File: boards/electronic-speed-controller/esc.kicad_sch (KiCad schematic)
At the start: 29 parts, among them J101 XT60PW-M, J102 39303037, K101 G5PZ-1A4-E, SW101 1825255-1, U101 LMR51420XDDCR, U102 Teensy4.1

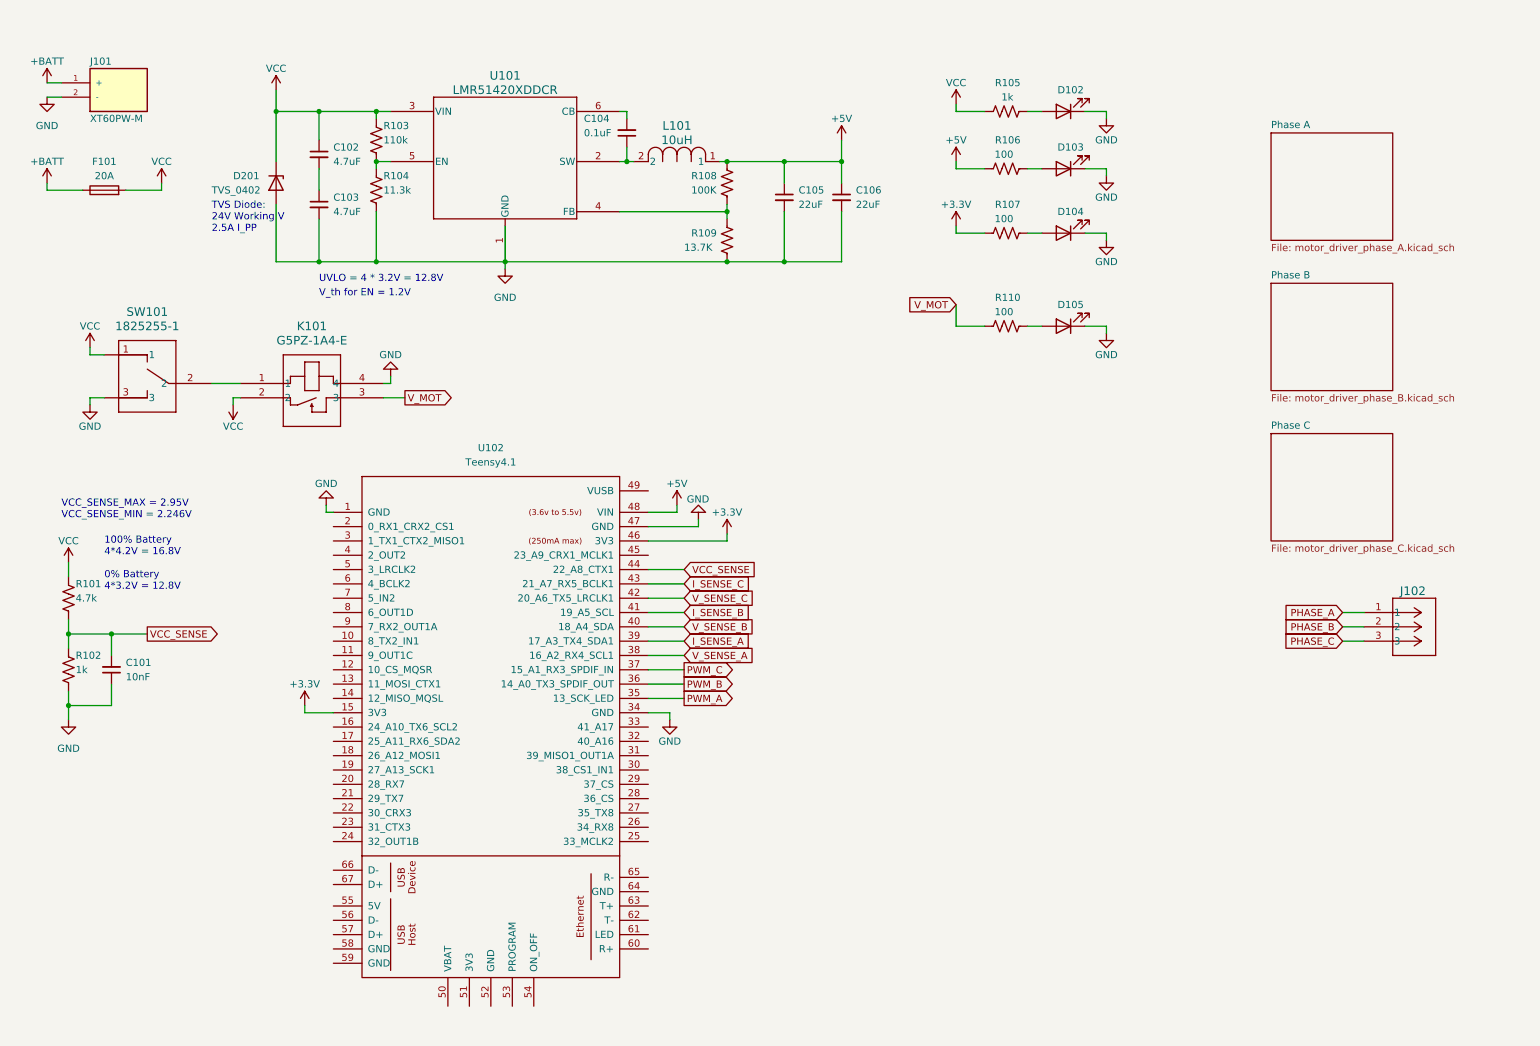
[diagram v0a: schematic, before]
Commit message: updated MOSFETs
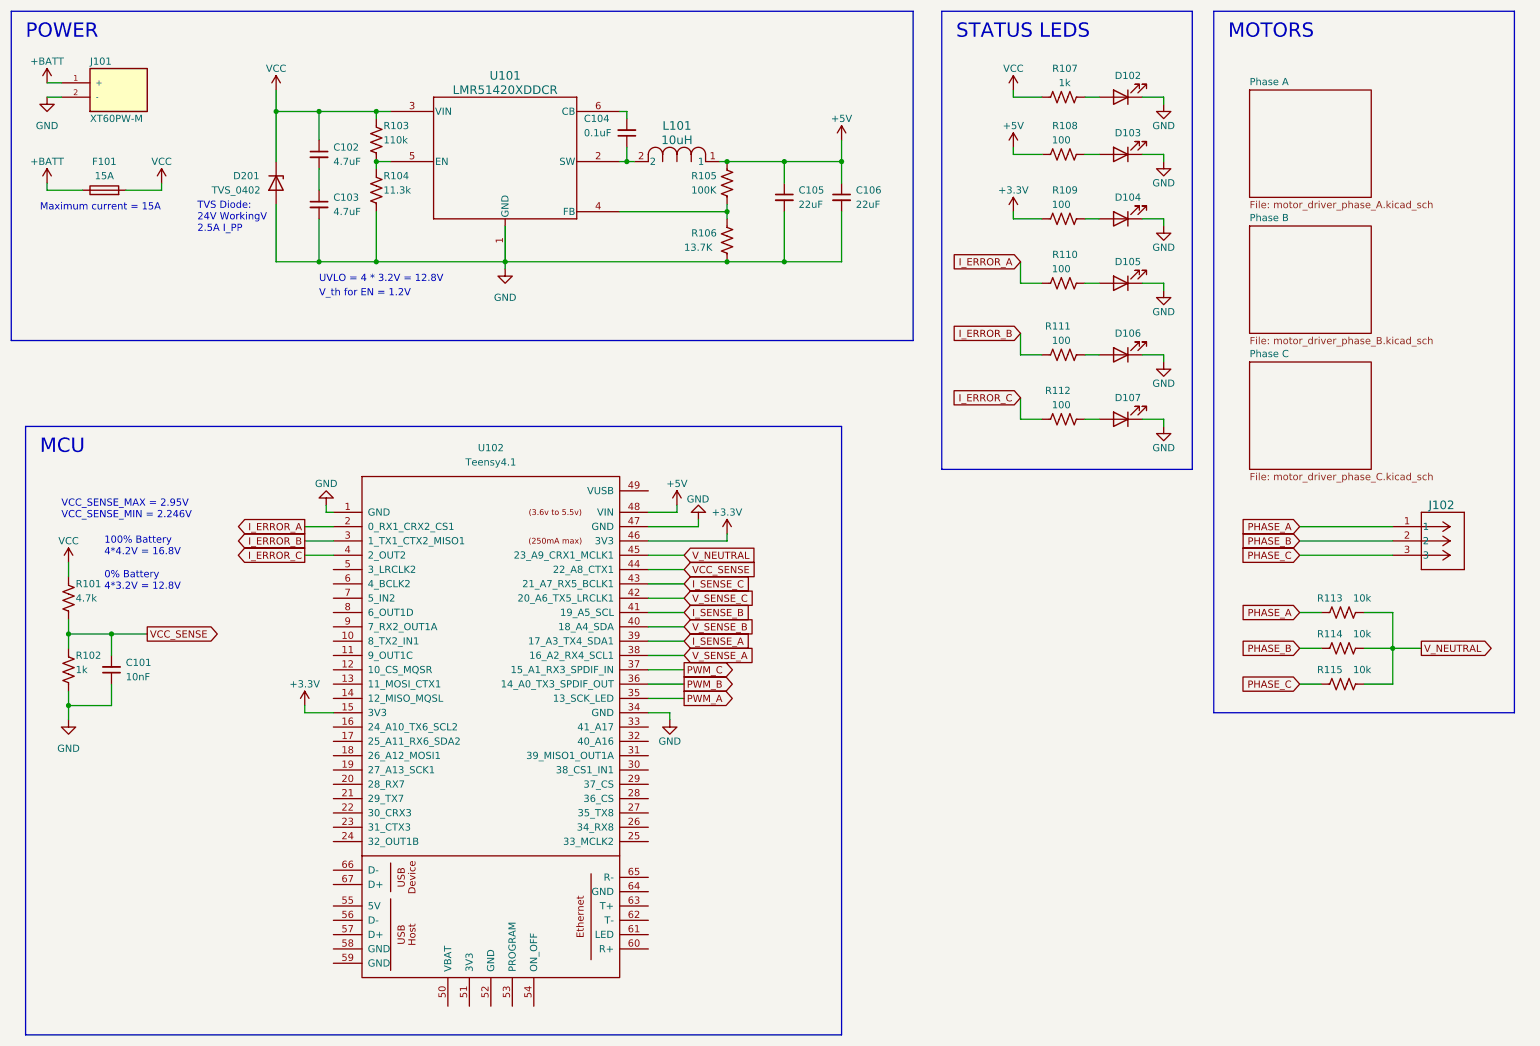
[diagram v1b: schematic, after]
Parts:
- removed K101: G5PZ-1A4-E, G5PZ_OMR, symbol Omron:G5PZ-1A4-E
- removed SW101: 1825255-1, SW3_1825255-1_TEC, symbol Slide_switch:1825255-1
- added D106, D107: LED, LED_SMD:LED_0201_0603Metric, symbol Device:LED
- added R111, R112: 100, Resistor_SMD:R_0603_1608Metric, symbol Device:R_US
- added R113, R114, R115: 10k, Resistor_SMD:R_0603_1608Metric, symbol Device:R_US
- D105: footprint LED_SMD:LED_2512_6332Metric -> LED_SMD:LED_0201_0603Metric
- F101: value 20A -> 15A
- renumbered R108 to R105, R109 to R106, R105 to R107, R106 to R108, R107 to R109
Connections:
- net V_MOT is gone; now on net I_ERROR_A: R110.1
- net GND: now also D106.1 (K), D107.1 (K)
- net PHASE_A: now also R113.1
- net PHASE_B: now also R114.1
- net PHASE_C: now also R115.1
- net I_ERROR_A: now reaches U102.2 (0_RX1_CRX2_CS1)
- net I_ERROR_B: now reaches U102.3 (1_TX1_CTX2_MISO1)
- net I_ERROR_B: now also R111.1
- net I_ERROR_C: now reaches U102.4 (2_OUT2)
- net I_ERROR_C: now also R112.1
- net V_NEUTRAL: now reaches U102.45 (23_A9_CRX1_MCLK1)
- net V_NEUTRAL: now also R113.2, R114.2, R115.2
- new net: D106.2 (A), R111.2
- new net: D107.2 (A), R112.2
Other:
- note added: "MCU"
- note added: "MOTORS"
- note added: "Maximum current = 15A"
- note added: "POWER"
- note added: "STATUS LEDS"
- note added: "TVS Diode: 24V WorkingV 2.5A I_PP"
- note removed: "TVS Diode: 24V Working V 2.5A I_PP"
- moved on the sheet: D102, D103, D104, J102, R107, R108, R109, R110

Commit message: finished layout and schematic
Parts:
- removed F101: 15A, Fuse:Fuse_1206_3216Metric, symbol Device:Fuse
- removed U102: Teensy4.1, teensy.pretty-master:Teensy41, symbol teensy:Teensy4.1
- added C107, C108, C109: 0.1uF, Capacitor_SMD:C_0603_1608Metric, symbol Device:C_Small
- added R116, R117, R118: 4.7k, Resistor_SMD:R_0603_1608Metric, symbol Device:R_US
- added U102, U104, U105: TL331, Package_TO_SOT_SMD:SOT-23-5, symbol Comparator:TL331
- added U103: Teensy4.0, teensy.pretty-master:Teensy40, symbol teensy:Teensy4.0
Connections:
- net +BATT is gone; now on net VCC: J101.1 (+)
- net +3.3V: now also R116.1, R117.1, R118.1, U103.16 (3V3), U103.31 (3V3)
- net +5V: now also U103.33 (VIN)
- net GND: now also C107.2, C108.2, C109.2, U102.2 (V-), U103.1 (GND), U103.17 (GND), U103.32 (GND), U104.2 (V-), U105.2 (V-)
- net I_ERROR_A: now also U103.2 (0_RX1_CRX2_CS1)
- net I_ERROR_B: now also U103.3 (1_TX1_CTX2_MISO1)
- net I_ERROR_C: now also U103.4 (2_OUT2)
- net I_SENSE_A: now also U103.29 (22_A8_CTX1)
- net I_SENSE_B: now also U103.25 (18_A4_SDA0)
- net I_SENSE_C: now also U103.21 (14_A0_TX3_SPDIF_OUT)
- net PHASE_A: now also U102.3 (+)
- net PHASE_B: now also U104.3 (+)
- net PHASE_C: now also U105.3 (+)
- net PWM_A: now also U103.28 (21_A7_RX5_BCLK1)
- net PWM_B: now also U103.24 (17_A3_TX4_SDA1)
- net PWM_C: now also U103.20 (13_SCK_CRX1_LED)
- net VCC: now also C107.1, C108.1, C109.1, U102.5 (V+), U104.5 (V+), U105.5 (V+)
- net VCC_SENSE: now also U103.14 (12_MISO_MQSL)
- net V_NEUTRAL: now also U102.1 (-), U104.1 (-), U105.1 (-)
- net V_SENSE_A: now also U103.30 (23_A9_CRX1_MCLK1)
- net V_SENSE_B: now also U103.26 (19_A5_SCL0)
- net V_SENSE_C: now also U103.22 (15_A1_RX3_SPDIF_IN)
- new net ZERO_A: R116.2, U102.4, U103.13 (11_MOSI_CTX1)
- new net ZERO_B: R117.2, U103.12 (10_CS_MQSR), U104.4
- new net ZERO_C: R118.2, U103.11 (9_OUT1C), U105.4
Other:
- note added: "ZERO CROSSING COMPARATORS"
- moved on the sheet: C101, C102, C103, C104, C105, C106, D102, D103, D104, D105, D106, D107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

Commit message: simplified PHASE A circuit
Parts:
- added C110: 0.1uF, Capacitor_SMD:C_0603_1608Metric, symbol Device:C_Small
- added C111: 1nF, Capacitor_SMD:C_0603_1608Metric, symbol Device:C_Small
- added R119: 2m, Resistor_SMD:R_2512_6332Metric, symbol Device:R_Small_US
- added R120: 1k, Resistor_SMD:R_0603_1608Metric, symbol Device:R_US
- added U106: INA180A3IDBVR, DBV0005A_N, symbol Current_Sense_Amp:INA180A3IDBVR
- D102, D103, D104, D105, D106, D107: footprint LED_SMD:LED_0201_0603Metric -> LED_SMD:LED_0603_1608Metric
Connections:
- net GND: now also C110.1, C111.1, R119.2, U106.2 (GND), U106.4 (IN-)
- net VCC: now also C110.2, R119.1, U106.3 (IN+), U106.5 (VS)
- net CURRENT_SENSE: now reaches U103.7 (5_IN2)
- net CURRENT_SENSE: now also C111.2, R120.2
- net I_SENSE_A: no longer names the net of U103.29 (22_A8_CTX1)
- net I_SENSE_B: no longer names the net of U103.25 (18_A4_SDA0)
- net I_SENSE_C: no longer names the net of U103.21 (14_A0_TX3_SPDIF_OUT)
- new net: R120.1, U106.1 (OUT)
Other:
- note added: "Current Sense"
- note added: "Gain = 100V/V V(I_PHASE_MAX) = 3V"
- note added: "I_PHASE_MAX = 15A V(Rs) = 0.03V P(Rs) = 15*15*1e^-3"
- note added: "Limit BW to 150 kHz"
